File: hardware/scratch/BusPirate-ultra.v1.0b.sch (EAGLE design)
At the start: 176 parts, among them IC1 23LC1024, IC10 SN74LVC1T45DBV, IC11 SN74LVC1T45DBV, IC12 74LVC1G07DBV, IC13 SN74LVC1T45DBV, IC17 74LVC1G07DBV, IC18 SN74LVC1T45DBV, IC19 74LVC1G07DBV, IC2 23LC1024, IC20 SN74LVC1T45DBV, IC21 74LVC1G07DBV, IC22 SN74LVC1T45DBV, IC23 MCP1824_ADJ, IC24 74HCT4051, IC3 74AC573, IC4 74LVC1G07DBV, IC5 74LVC1G07DBV, IC6 74LVC1G07DBV, IC7 74LVC1G07DBV, IC8 SN74LVC1T45DBV, IC9 SN74LVC1T45DBV, J2 CON_HEADER_1X04, J4 CON_HEADER_1X10-RIGHT_ANGLED_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, Q1 DMMT3906W, U1 W25X40CL, U2 STM32F103ZX, U3 ICE40HX4K, U4 MCP6001, U5 MCP4442, U6 MCP4442, U7 MCP6001

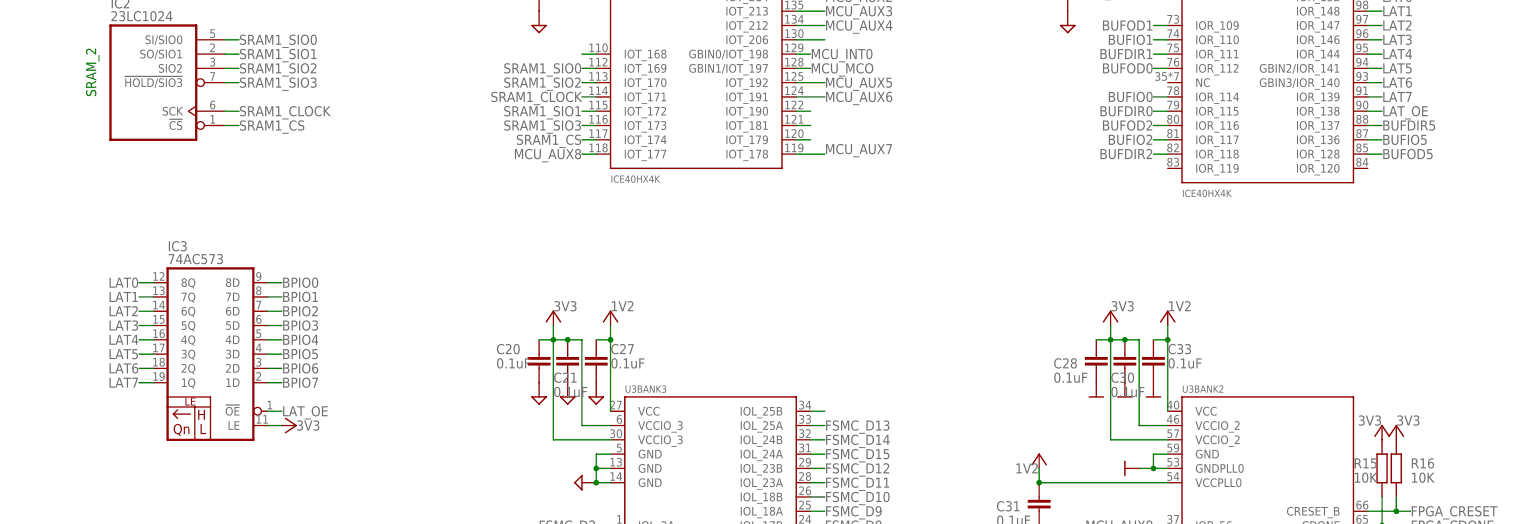
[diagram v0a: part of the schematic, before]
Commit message: latch's OE tied to gnd, move things around
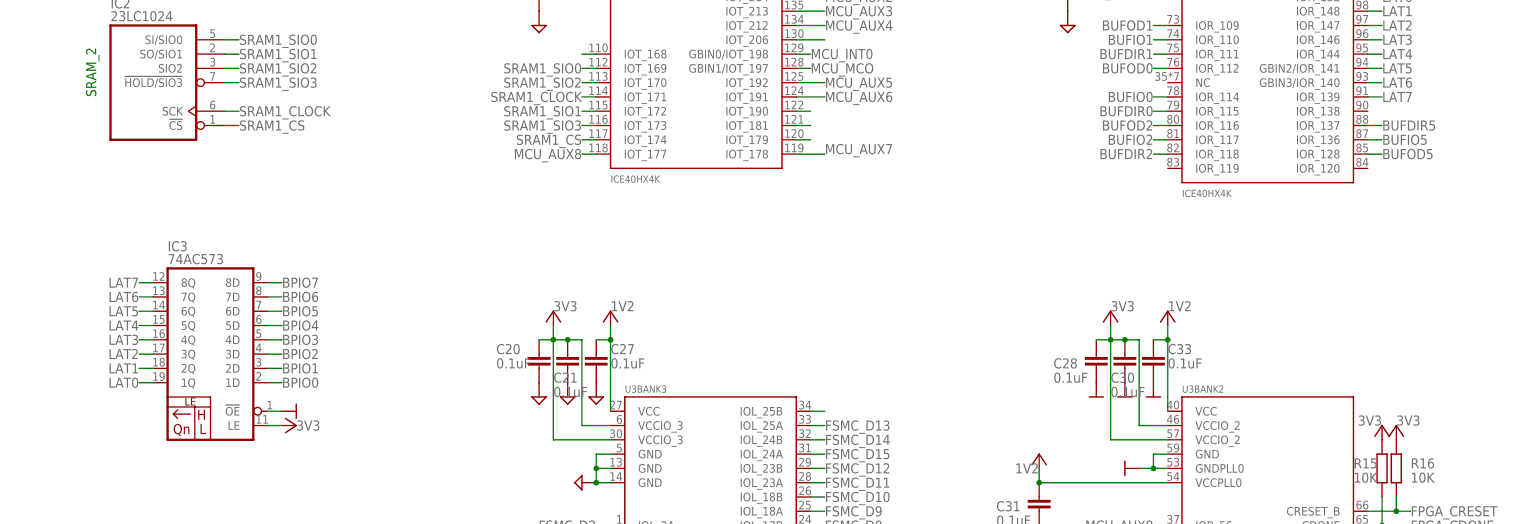
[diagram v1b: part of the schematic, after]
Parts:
- C55, C56, C57, C58, C59, C60: device rcl:C-EUC0603 -> resistor:C-EUC0402
- IC10, IC11, IC13, IC18, IC20, IC22, IC8, IC9: device dp_devices.v6:IC_BUFF_SN74LVC1T45DBV-SC-70-6 -> dp_devices.v6:IC_BUFF_SN74LVC1T45DBV-EXTENDED
- IC12, IC17, IC19, IC21, IC4, IC5, IC6, IC7: device dp_devices.v6:IC_BUFF_74LVC1G07 -> dp_devices.v6:IC_BUFF_74LVC1G07-EXTENDED
- R34, R35, R36, R37, R38, R39, R41, R42: device rcl:R-EU_R0603 -> resistor:R-EU_R0402
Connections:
- removed net LAT_OE: IC3IC.!OE, U3BANK1.IOR_138
- net BPIO0: now also IC3IC.1D; no longer IC3IC.8D
- net BPIO1: now also IC3IC.2D; no longer IC3IC.7D
- net BPIO2: now also IC3IC.3D; no longer IC3IC.6D
- net BPIO3: now also IC3IC.4D; no longer IC3IC.5D
- net BPIO4: now also IC3IC.5D; no longer IC3IC.4D
- net BPIO5: now also IC3IC.6D; no longer IC3IC.3D
- net BPIO6: now also IC3IC.7D; no longer IC3IC.2D
- net BPIO7: now also IC3IC.8D; no longer IC3IC.1D
- net GND: now also IC3IC.!OE
- net LAT0: now also IC3IC.1Q; no longer IC3IC.8Q
- net LAT1: now also IC3IC.2Q; no longer IC3IC.7Q
- net LAT2: now also IC3IC.3Q; no longer IC3IC.6Q
- net LAT3: now also IC3IC.4Q; no longer IC3IC.5Q
- net LAT4: now also IC3IC.5Q; no longer IC3IC.4Q
- net LAT5: now also IC3IC.6Q; no longer IC3IC.3Q
- net LAT6: now also IC3IC.7Q; no longer IC3IC.2Q
- net LAT7: now also IC3IC.8Q; no longer IC3IC.1Q

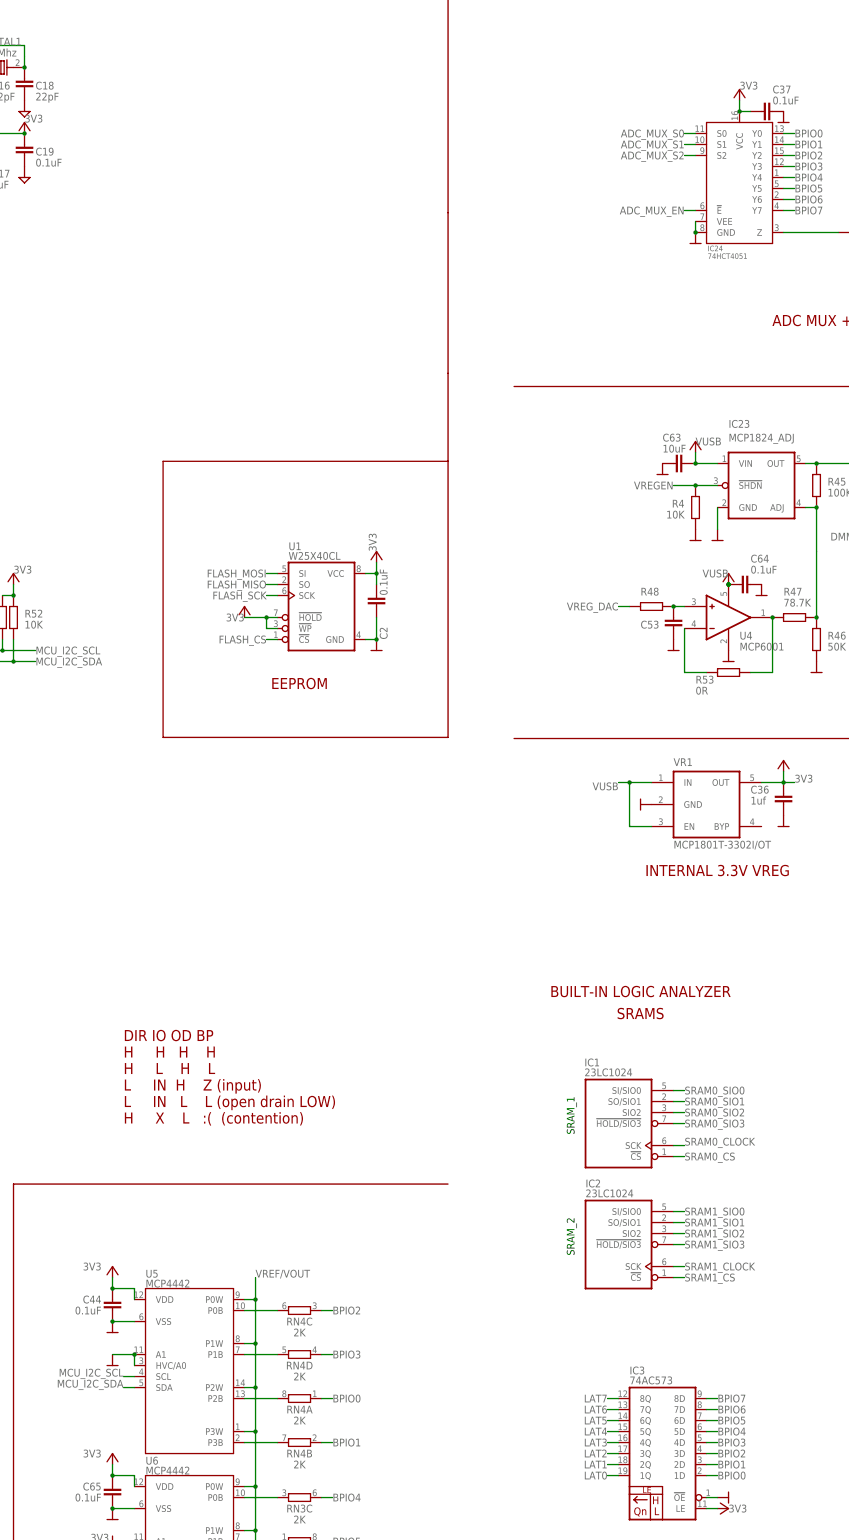
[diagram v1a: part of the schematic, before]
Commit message: ADC mux chip 4051 Vcc connected to VUSB, digital pots (MCP4442) supply vdd connected to VUSB
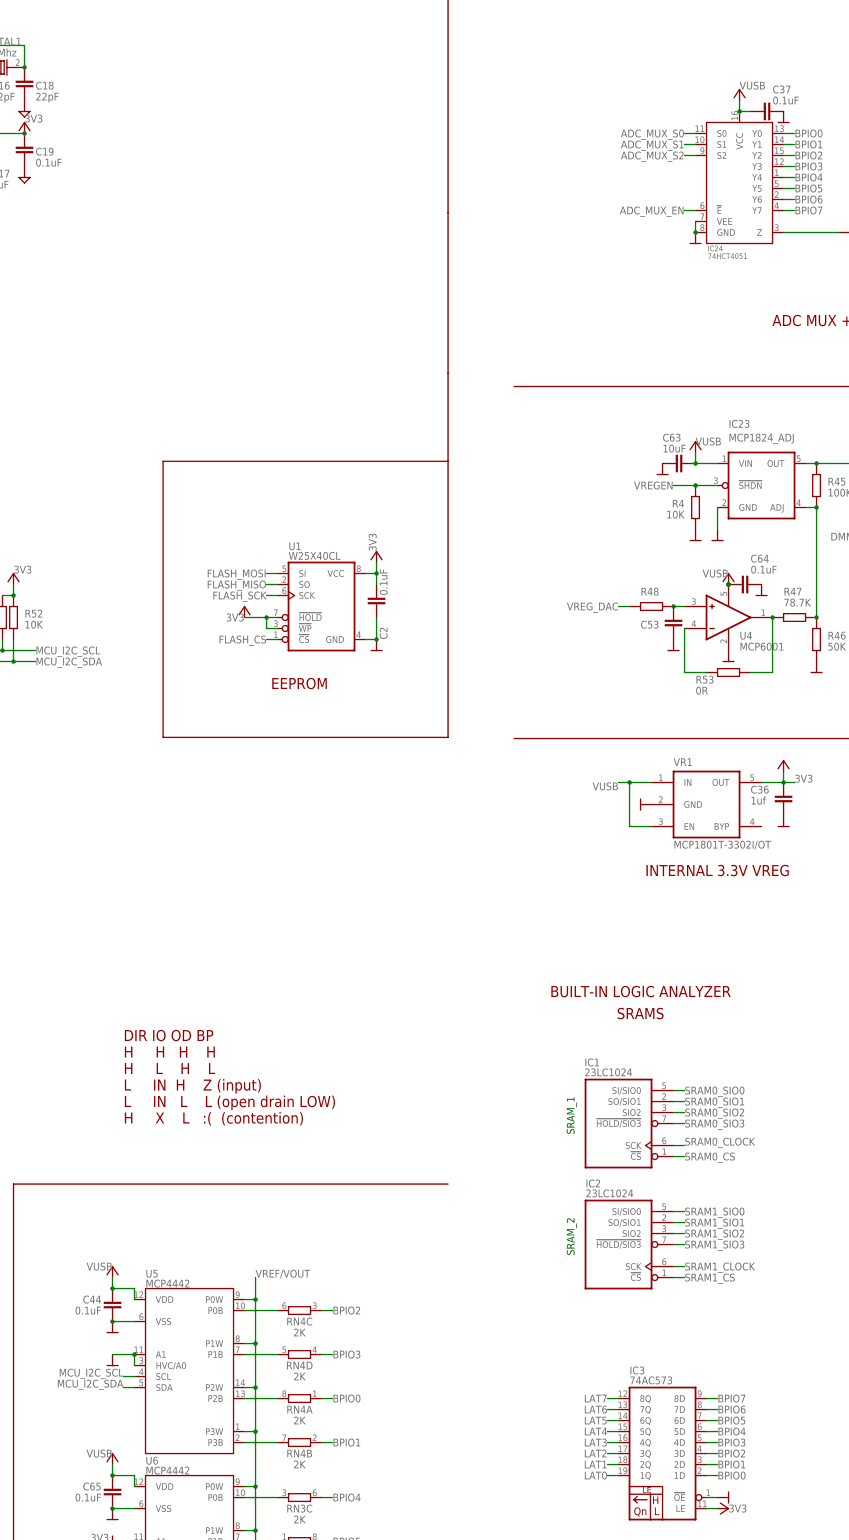
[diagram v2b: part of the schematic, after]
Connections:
- net 3V3: no longer C37.1, C44.1, C65.1, IC24.VCC, U5.VDD, U6.VDD
- net VUSB: now also C37.1, C44.1, C65.1, IC24.VCC, U5.VDD, U6.VDD
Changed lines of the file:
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@@
-</segment>
-<segment>
-<pinref part="C37" gate="G$1" pin="1"/>
-<wire x1="342.9" y1="408.94" x2="340.36" y2="408.94" width="0.1524" layer="91"/>
-<pinref part="IC24" gate="IC" pin="VCC"/>
-<wire x1="340.36" y1="408.94" x2="340.36" y2="411.48" width="0.1524" layer="91"/>
-<junction x="340.36" y="408.94"/>
-<pinref part="SUPPLY61" gate="1" pin="V+"/>
-<label x="340.36" y="414.02" size="1.778" layer="95"/>
-</segment>
-<segment>
-<pinref part="C44" gate="G$1" pin="1"/>
-<wire x1="195.58" y1="137.16" x2="200.66" y2="137.16" width="0.1524" layer="91"/>
-<pinref part="U5" gate="U" pin="VDD"/>
-<wire x1="200.66" y1="137.16" x2="200.66" y2="134.62" width="0.1524" layer="91"/>
-<pinref part="SUPPLY76" gate="1" pin="V+"/>
-<wire x1="195.58" y1="137.16" x2="195.58" y2="139.7" width="0.1524" layer="91"/>
-<junction x="195.58" y="137.16"/>
-<label x="193.04" y="142.24" size="1.778" layer="95" align="center-right"/>
-</segment>
-<segment>
-<pinref part="C65" gate="G$1" pin="1"/>
-<wire x1="195.58" y1="93.98" x2="200.66" y2="93.98" width="0.1524" layer="91"/>
-<pinref part="U6" gate="U" pin="VDD"/>
-<wire x1="200.66" y1="93.98" x2="200.66" y2="91.44" width="0.1524" layer="91"/>
-<pinref part="SUPPLY95" gate="1" pin="V+"/>
-<wire x1="195.58" y1="93.98" x2="195.58" y2="96.52" width="0.1524" layer="91"/>
-<junction x="195.58" y="93.98"/>
-<label x="193.04" y="99.06" size="1.778" layer="95" align="center-right"/>
 </segment>
 <segment>
@@
 <label x="330.2" y="332.74" size="1.778" layer="95" rot="R180" align="center-right"/>
 </segment>
-</net>
+<segment>
+<pinref part="C37" gate="G$1" pin="1"/>
+<wire x1="342.9" y1="408.94" x2="340.36" y2="408.94" width="0.1524" layer="91"/>
+<pinref part="IC24" gate="IC" pin="VCC"/>
+<wire x1="340.36" y1="408.94" x2="340.36" y2="411.48" width="0.1524" layer="91"/>
+<junction x="340.36" y="408.94"/>
+<pinref part="SUPPLY61" gate="1" pin="V+"/>
+<label x="340.36" y="414.02" size="1.778" layer="95"/>
+</segment>
+<segment>
+<pinref part="C44" gate="G$1" pin="1"/>
+<wire x1="195.58" y1="137.16" x2="200.66" y2="137.16" width="0.1524" layer="91"/>
+<pinref part="U5" gate="U" pin="VDD"/>
+<wire x1="200.66" y1="137.16" x2="200.66" y2="134.62" width="0.1524" layer="91"/>
+<pinref part="SUPPLY76" gate="1" pin="V+"/>
+<wire x1="195.58" y1="137.16" x2="195.58" y2="139.7" width="0.1524" layer="91"/>
+<junction x="195.58" y="137.16"/>
+<label x="195.58" y="142.24" size="1.778" layer="95" align="center-right"/>
+</segment>
+<segment>
+<pinref part="C65" gate="G$1" pin="1"/>
+<wire x1="195.58" y1="93.98" x2="200.66" y2="93.98" width="0.1524" layer="91"/>
+<pinref part="U6" gate="U" pin="VDD"/>
+<wire x1="200.66" y1="93.98" x2="200.66" y2="91.44" width="0.1524" layer="91"/>
+<pinref part="SUPPLY95" gate="1" pin="V+"/>
+<wire x1="195.58" y1="93.98" x2="195.58" y2="96.52" width="0.1524" layer="91"/>
+<junction x="195.58" y="93.98"/>
+<label x="195.58" y="99.06" size="1.778" layer="95" align="center-right"/>
+</segment>
+</net>

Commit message: change buffer 573 to 244, replaced MCP4446 digital pot back to 4066 analog switch
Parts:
- removed IC3: 74AC573, dp_devices:IC_74AC573-TSSOP-20
- removed R49, R52: 10K, dp_devices.v6:RESISTOR-0603
- removed U6: MCP4442, dp_devices.v6:IC_MCP4442
- added U8, U9: 74HCT4066PW, dp_devices.v6:IC_74HCT4066PW
- U5: value MCP4442 -> 74LVC245A; device dp_devices.v6:IC_MCP4442 -> dp_devices.v6:IC_BUFF_74LVC245A-TSSOP20
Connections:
- removed net MCU_I2C_SCL: R49.1, U2U.I2C1_SCL('0')/TIM4_CH1('0')/USART1_TX('1')/FT/PB6, U5.SCL, U6.SCL
- removed net MCU_I2C_SDA: R52.1, U2U.I2C1_SDA('0')/FSMC_NADV/TIM4_CH2('0')/USART1_RX('1')/FT/PB7, U5.SDA, U6.SDA
- removed net N$47: RN3B.1, U6.P2B
- removed net N$48: RN3D.1, U6.P3B
- removed net V33PU: U2U.PG0/FT/FSMC_A10
- removed net V50PU: U2U.PG1/FT/FSMC_A11
- new net MCU_VPU: U2U.PG0/FT/FSMC_A10, U8A.E, U8B.E, U8C.E, U8D.E, U9A.E, U9B.E, U9C.E, U9D.E
- new net N$33: RN3C.1, U9A.Y
- new net N$45: RN3D.1, U9D.Y
- net 3V3: now also U5SUPPLY.V+; no longer IC3IC.LE, IC3PWR.V+, R49.2, R52.2, U6.HVC/A0
- net BPIO0: now also U5G$1.B7; no longer IC3IC.1D
- net BPIO1: now also U5G$1.B6; no longer IC3IC.2D
- net BPIO2: now also U5G$1.B5; no longer IC3IC.3D
- net BPIO3: now also U5G$1.B4; no longer IC3IC.4D
- net BPIO4: now also U5G$1.B3; no longer IC3IC.5D
- net BPIO5: now also U5G$1.B2; no longer IC3IC.6D
- net BPIO6: now also U5G$1.B1; no longer IC3IC.7D
- net BPIO7: now also U5G$1.B0; no longer IC3IC.8D
- net GND: now also U5G$1.!OE, U5G$1.DIR, U5SUPPLY.GND, U8SUP.GND, U9SUP.GND; no longer IC3IC.!OE, IC3PWR.GND, U5.A1, U5.HVC/A0, U5.VSS, U6.A1, U6.VSS
- net LAT0: now also U5G$1.A7; no longer IC3IC.1Q
- net LAT1: now also U5G$1.A6; no longer IC3IC.2Q
- net LAT2: now also U5G$1.A5; no longer IC3IC.3Q
- net LAT3: now also U5G$1.A4; no longer IC3IC.4Q
- net LAT4: now also U5G$1.A3; no longer IC3IC.5Q
- net LAT5: now also U5G$1.A2; no longer IC3IC.6Q
- net LAT6: now also U5G$1.A1; no longer IC3IC.7Q
- net LAT7: now also U5G$1.A0; no longer IC3IC.8Q
- net N$2: now also U8A.Y; no longer U5.P0B
- net N$3: now also U8B.Y; no longer U5.P1B
- net N$4: now also U8C.Y; no longer U5.P2B
- net N$42: now also RN3A.1, U9B.Y; no longer RN3C.1, U6.P0B
- net N$44: now also RN3B.1, U9C.Y; no longer RN3A.1, U6.P1B
- net N$5: now also U8D.Y; no longer U5.P3B
- net VREF/VOUT: now also U8A.Z, U8B.Z, U8C.Z, U8D.Z, U9A.Z, U9B.Z, U9C.Z, U9D.Z; no longer U5.P0W, U5.P1W, U5.P2W, U5.P3W, U6.P0W, U6.P1W, U6.P2W, U6.P3W
- net VUSB: now also U8SUP.V+, U9SUP.V+; no longer U5.VDD, U6.VDD
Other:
- moved on the sheet: C44, C65, RN3A, RN3B, RN3C, RN3D, RN4A, RN4B, RN4C, RN4D
